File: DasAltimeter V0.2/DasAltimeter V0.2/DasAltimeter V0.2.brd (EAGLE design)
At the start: 38.9 x 21.6 mm, 53 parts, among them IC1 BMI055, U1 ATSAMD21G-A, U2 3.3V/150mA, U3 MS5803-14BA, U4 ADXL193, X1 22-23-2041, X2 22-23-2041

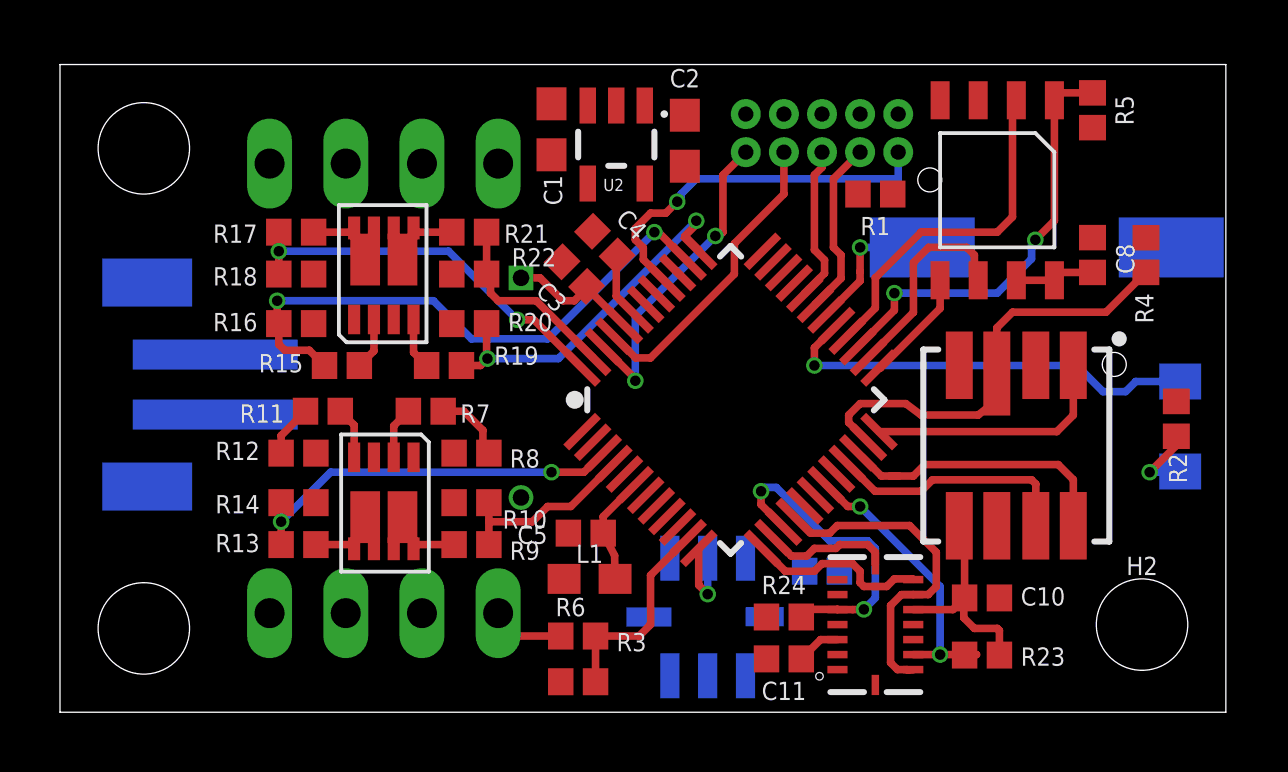
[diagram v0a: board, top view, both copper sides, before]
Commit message: boards sent to fab
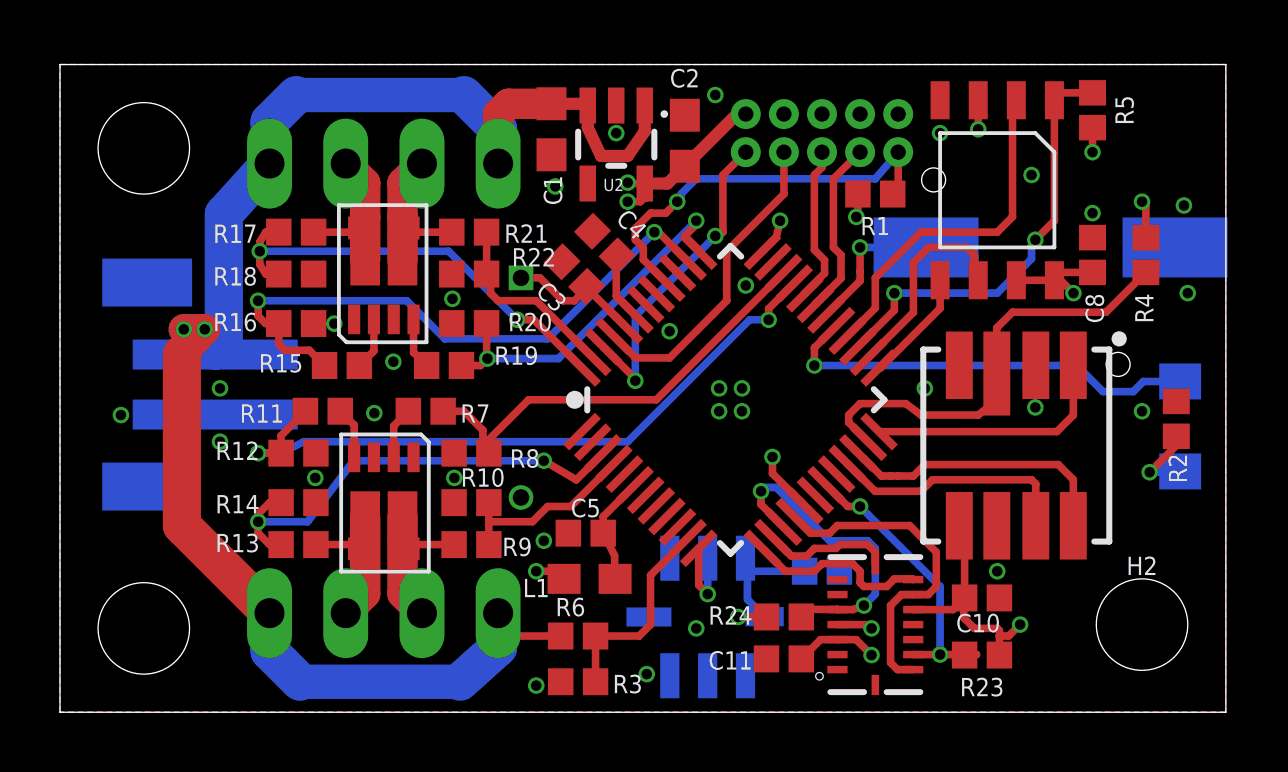
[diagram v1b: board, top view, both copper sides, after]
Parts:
- moved SG1 0.13 mm to (33.0, 15.5)
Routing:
- net VCC: track 2.77 -> 54.4 mm, vias 0 -> 2
- net 3.3V: track 15.8 -> 38.1 mm, vias 0 -> 13
- net FIRE_D: track 1.73 -> 22.9 mm, vias 0 -> 2
- net FIRE_C: track 2.43 -> 14.8 mm
- net FET_D: track 1.33 -> 6.67 mm
- net FET_C: track 1.41 -> 6.60 mm
- net FET_A: track 1.41 -> 5.89 mm
- net FET_B: track 1.33 -> 5.81 mm
- net SENSE_D: track 13.1 -> 15.5 mm
- net SENSE_A: track 13.1 -> 14.7 mm
- net GND: track 0.00 -> 1.26 mm, vias 0 -> 32
- net FIRE_A: track 19.4 -> 20.6 mm
- net !RESET: track 12.7 -> 13.7 mm
- added copper zone on layer 15, net 3.3V
- added copper zone on layer 1, net GND
- added copper zone on layer 16, net GND
- added copper zone on layer 2, net GND
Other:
- board text added: "A"
- board text added: "B"
- board text added: "C"
- board text added: "D"
